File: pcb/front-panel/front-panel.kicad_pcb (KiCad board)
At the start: 2 copper layers, 165 x 51.1 mm, 1 part

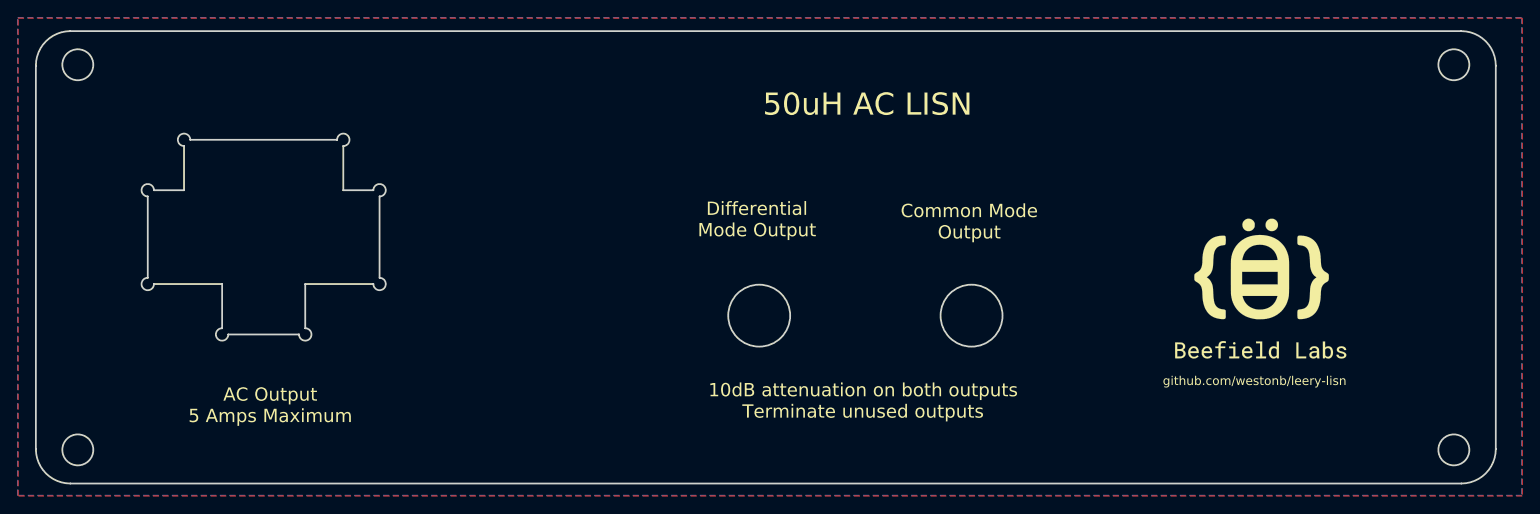
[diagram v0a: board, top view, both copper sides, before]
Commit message: Bump to KiCad 8, add BOM info
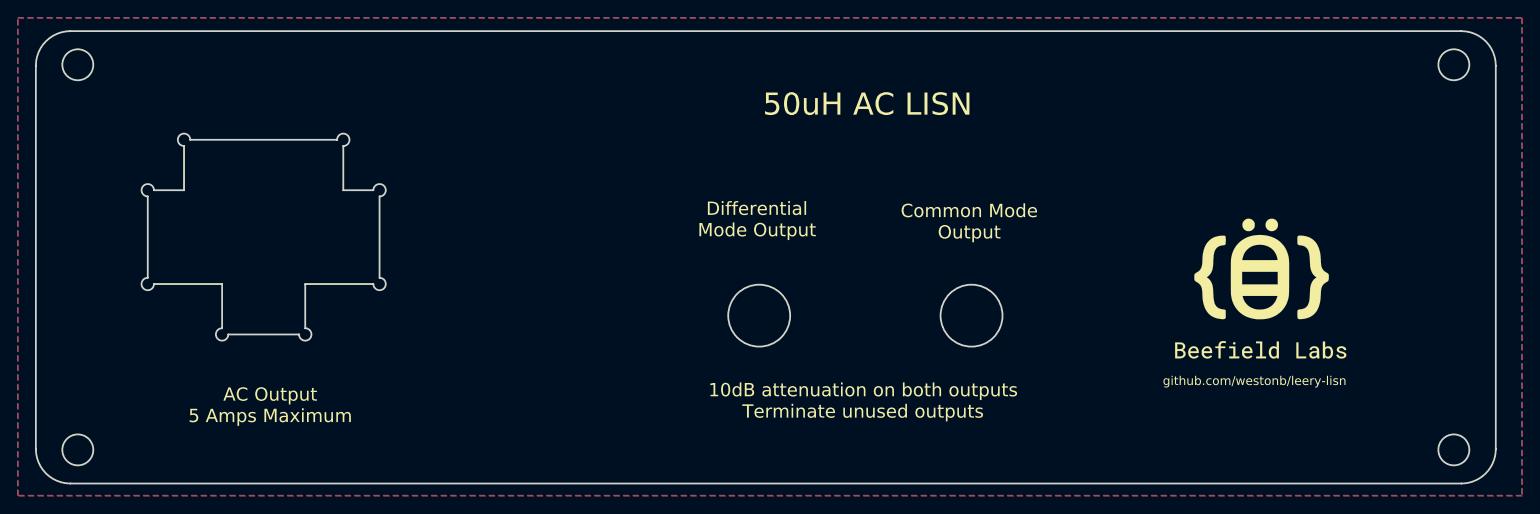
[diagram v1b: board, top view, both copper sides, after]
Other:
- net class Default removed
